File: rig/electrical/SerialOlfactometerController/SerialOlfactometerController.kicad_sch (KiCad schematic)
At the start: 34 parts, among them J1 Screw_Terminal_01x02, J10 Screw_Terminal_01x02, J11 Screw_Terminal_01x02, J12 Screw_Terminal_01x02, J13 Screw_Terminal_01x02, J14 Screw_Terminal_01x02, J15 Screw_Terminal_01x02, J16 Screw_Terminal_01x02, J17 Conn_01x05_Socket, J18 TST-105-01-X-D, J19 TST-105-01-X-D, J2 Screw_Terminal_01x02, J3 Screw_Terminal_01x02, J4 Screw_Terminal_01x02, J5 Screw_Terminal_01x02, J6 Screw_Terminal_01x02, J7 Screw_Terminal_01x02, J8 Screw_Terminal_01x02, J9 Screw_Terminal_01x02, U1 TPIC6595, U2 TPIC6595

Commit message: Serial Olfactometer improved design
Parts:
- added TP1, TP2, TP3, TP4, TP5, TP6: TestPoint, TestPoint:TestPoint_Pad_2.0x2.0mm, symbol Connector:TestPoint
- R3, R4, R5, R6, R7: value R -> 33Ω
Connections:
- net at J19.01, R7.2, U1.13 (SRCK)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: now also TP2.1, TP6.1
- net at J17.5 (Pin_5), U1.12 (RCLK), U2.12 (RCLK): now also TP3.1
- net at U1.18 (SER_OUT), U2.3 (SER_IN): now also TP4.1
- net at J18.03, U1.3 (SER_IN): now also TP1.1
- net at J19.03, U2.18 (SER_OUT): now also TP5.1
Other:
- company: (none) -> Ruta and Kronauer Labs, Rockefeller University
- title: (none) -> MultiBiOS Serial Olfactometer Controller
- moved on the sheet: C1, C2, C3, C4, H1, H2, J1, J10, J11, J12, J13, J14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

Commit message: Update SerialOlfactometerController.kicad_sch
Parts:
- removed H1, H2: MountingHole, MountingHole:MountingHole_3.2mm_M3_DIN965_Pad, symbol Mechanical:MountingHole
- added H3, H4: MountingHole_Pad, symbol Mechanical:MountingHole_Pad
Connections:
- net GND: now also H3.1, H4.1
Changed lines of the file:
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@@
 	)
 	(junction
+		(at 170.18 157.48)
+		(diameter 0)
+		(color 0 0 0 0)
+	)
+	(junction
 		(at 130.81 153.67)
 		(diameter 0)
@@
 	(wire
 		(pts
+			(xy 163.83 157.48) (xy 163.83 158.75)
+		)
+		(stroke
+			(width 0)
+			(type default)
+		)
+	)
+	(wire
+		(pts
 			(xy 114.3 137.16) (xy 114.3 133.35)
 		)
@@
 	(wire
 		(pts
+			(xy 170.18 157.48) (xy 163.83 157.48)
+		)
+		(stroke
+			(width 0)
+			(type default)
+		)
+	)
+	(wire
+		(pts
 			(xy 50.8 158.75) (xy 50.8 165.1)
 		)
@@
 	(wire
 		(pts
+			(xy 173.99 166.37) (xy 170.18 166.37)
+		)
+		(stroke
+			(width 0)
+			(type default)
+		)
+	)
+	(wire
+		(pts
 			(xy 156.21 130.81) (xy 175.26 130.81)
 		)
@@
 	(wire
 		(pts
+			(xy 173.99 157.48) (xy 170.18 157.48)
+		)
+		(stroke
+			(width 0)
+			(type default)
+		)
+	)
+	(wire
+		(pts
 			(xy 91.44 172.72) (xy 91.44 186.69)
 		)
@@
 	(wire
 		(pts
+			(xy 170.18 157.48) (xy 170.18 166.37)
+		)
+		(stroke
+			(width 0)
+			(type default)
+		)
+	)
+	(wire
+		(pts
 			(xy 50.8 165.1) (xy 52.07 165.1)
 		)
@@
 	)
 	(symbol
+		(lib_id "power:GND")
+		(at 163.83 158.75 0)
+		(unit 1)
+		(exclude_from_sim no)
+		(in_bom yes)
+		(on_board yes)
+		(dnp no)
+		(fields_autoplaced yes)
+		(property "Reference" "#PWR035"
+			(at 163.83 165.1 0)
+			(effects
+				(font
+					(size 1.27 1.27)
+				)
+				(hide yes)
+			)
+		)
+		(property "Value" "GND"
+			(at 163.83 163.83 0)
+			(effects
+				(font
+					(size 1.27 1.27)
+				)
+			)
+		)
+		(property "Footprint" ""
+			(at 163.83 158.75 0)
+			(effects
+				(font
+					(size 1.27 1.27)
+				)
+				(hide yes)
+			)
+		)
+		(property "Datasheet" ""
+			(at 163.83 158.75 0)
+			(effects
+				(font
+					(size 1.27 1.27)
+				)
+				(hide yes)
+			)
+		)
+		(property "Description" "Power symbol creates a global label with name \"GND\" , ground"
+			(at 163.83 158.75 0)
+			(effects
+				(font
+					(size 1.27 1.27)
+				)
+				(hide yes)
+			)
+		)
+		(pin "1"
+		)
+		(instances
+			(project "SerialOlfactometerController"
+				(path "/50fb9429-008b-4a20-9c95-cf3891060a53"
+					(reference "#PWR035")
+					(unit 1)
+				)
+			)
+		)
+	)
+	(symbol
 		(lib_id "Connector:Screw_Terminal_01x02")
 		(at 118.11 77.47 90)
@@
 	)
 	(symbol
-		(lib_id "Mechanical:MountingHole")
-		(at 151.13 161.29 0)
-		(unit 1)
-		(exclude_from_sim no)
-		(in_bom no)
-		(on_board yes)
-		(dnp no)
-		(fields_autoplaced yes)
-		(property "Reference" "H2"
-			(at 153.67 160.0199 0)
-			(effects
-				(font
-					(size 1.27 1.27)
-				)
-				(justify left)
-			)
-		)
-		(property "Value" "MountingHole"
-			(at 153.67 162.5599 0)
-			(effects
-				(font
-					(size 1.27 1.27)
-				)
-				(justify left)
-			)
-		)
-		(property "Footprint" "MountingHole:MountingHole_3.2mm_M3_DIN965_Pad"
-			(at 151.13 161.29 0)
-			(effects
-				(font
-					(size 1.27 1.27)
-				)
-				(hide yes)
-			)
-		)
-		(property "Datasheet" "~"
-			(at 151.13 161.29 0)
-			(effects
-				(font
-					(size 1.27 1.27)
-				)
-				(hide yes)
-			)
-		)
-		(property "Description" "Mounting Hole without connection"
-			(at 151.13 161.29 0)
-			(effects
-				(font
-					(size 1.27 1.27)
-				)
-				(hide yes)
-			)
-		)
-		(instances
-			(project ""
-				(path "/50fb9429-008b-4a20-9c95-cf3891060a53"
-					(reference "H2")
-					(unit 1)
-				)
-			)
-		)
-	)
-	(symbol
 		(lib_id "Connector:TestPoint")
 		(at 130.81 153.67 0)
@@
 	)
 	(symbol
-		(lib_id "Mechanical:MountingHole")
-		(at 151.13 153.67 0)
-		(unit 1)
-		(exclude_from_sim no)
-		(in_bom no)
-		(on_board yes)
-		(dnp no)
-		(fields_autoplaced yes)
-		(property "Reference" "H1"
-			(at 153.67 152.3999 0)
-			(effects
-				(font
-					(size 1.27 1.27)
-				)
-				(justify left)
-			)
-		)
-		(property "Value" "MountingHole"
-			(at 153.67 154.9399 0)
-			(effects
-				(font
-					(size 1.27 1.27)
-				)
-				(justify left)
-			)
-		)
-		(property "Footprint" "MountingHole:MountingHole_3.2mm_M3_DIN965_Pad"
-			(at 151.13 153.67 0)
-			(effects
-				(font
-					(size 1.27 1.27)
-				)
-				(hide yes)
-			)
-		)
-		(property "Datasheet" "~"
-			(at 151.13 153.67 0)
-			(effects
-				(font
-					(size 1.27 1.27)
-				)
-				(hide yes)
-			)
-		)
-		(property "Description" "Mounting Hole without connection"
-			(at 151.13 153.67 0)
-			(effects
-				(font
-					(size 1.27 1.27)
-				)
-				(hide yes)
-			)
-		)
-		(instances
-			(project ""
-				(path "/50fb9429-008b-4a20-9c95-cf3891060a53"
-					(reference "H1")
-					(unit 1)
-				)
-			)
-		)
-	)
-	(symbol
 		(lib_id "Connector:Screw_Terminal_01x02")
 		(at 124.46 80.01 90)
@@
 	)
 	(symbol
+		(lib_id "Mechanical:MountingHole_Pad")
+		(at 173.99 154.94 0)
+		(unit 1)
+		(exclude_from_sim no)
+		(in_bom no)
+		(on_board yes)
+		(dnp no)
+		(fields_autoplaced yes)
+		(property "Reference" "H3"
+			(at 176.53 152.3999 0)
+			(effects
+				(font
+					(size 1.27 1.27)
+				)
+				(justify left)
+			)
+		)
+		(property "Value" "MountingHole_Pad"
+			(at 176.53 154.9399 0)
+			(effects
+				(font
+					(size 1.27 1.27)
+				)
+				(justify left)
+			)
+		)
+		(property "Footprint" ""
+			(at 173.99 154.94 0)
+			(effects
+				(font
+					(size 1.27 1.27)
+				)
+				(hide yes)
+			)
+		)
+		(property "Datasheet" "~"
+			(at 173.99 154.94 0)
+			(effects
+				(font
+					(size 1.27 1.27)
+				)
+				(hide yes)
+			)
+		)
+		(property "Description" "Mounting Hole with connection"
+			(at 173.99 154.94 0)
+			(effects
+				(font
+					(size 1.27 1.27)
+				)
+				(hide yes)
+			)
+		)
+		(pin "1"
+		)
+		(instances
+			(project ""
+				(path "/50fb9429-008b-4a20-9c95-cf3891060a53"
+					(reference "H3")
+					(unit 1)
+				)
+			)
+		)
+	)
+	(symbol
 		(lib_id "Connector:Screw_Terminal_01x02")
 		(at 111.76 85.09 90)
@@
 					(unit 1)
 				)
+			)
+		)
+	)
+	(symbol
+		(lib_id "Mechanical:MountingHole_Pad")
+		(at 173.99 163.83 0)
+		(unit 1)
+		(exclude_from_sim no)
+		(in_bom no)
+		(on_board yes)
+		(dnp no)
+		(fields_autoplaced yes)
+		(property "Reference" "H4"
+			(at 176.53 161.2899 0)
+			(effects
+				(font
+					(size 1.27 1.27)
+				)
+				(justify left)
+			)
+		)
+		(property "Value" "MountingHole_Pad"
+			(at 176.53 163.8299 0)
+			(effects
+				(font
+					(size 1.27 1.27)
+				)
+				(justify left)
+			)
+		)
+		(property "Footprint" ""
+			(at 173.99 163.83 0)
+			(effects
+				(font
+					(size 1.27 1.27)
+				)
+				(hide yes)
+			)
+		)
+		(property "Datasheet" "~"
+			(at 173.99 163.83 0)
+			(effects
+				(font
+					(size 1.27 1.27)
+				)
+				(hide yes)
+			)
+		)
+		(property "Description" "Mounting Hole with connection"
+			(at 173.99 163.83 0)
+			(effects
+				(font
+					(size 1.27 1.27)
+				)
+				(hide yes)
+			)
+		)
+		(pin "1"
+		)
+		(instances
+			(project ""
+				(path "/50fb9429-008b-4a20-9c95-cf3891060a53"
+					(reference "H4")
+					(unit 1)
+				)

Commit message: Tweaking of v1 boards
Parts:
- H3, H4: footprint (none) -> MountingHole:MountingHole_3.2mm_M3_Pad
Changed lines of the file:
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@@
 			)
 		)
-		(property "Footprint" ""
+		(property "Footprint" "MountingHole:MountingHole_3.2mm_M3_Pad"
 			(at 173.99 154.94 0)
 			(effects
@@
 			)
 		)
-		(property "Footprint" ""
+		(property "Footprint" "MountingHole:MountingHole_3.2mm_M3_Pad"
 			(at 173.99 163.83 0)
 			(effects

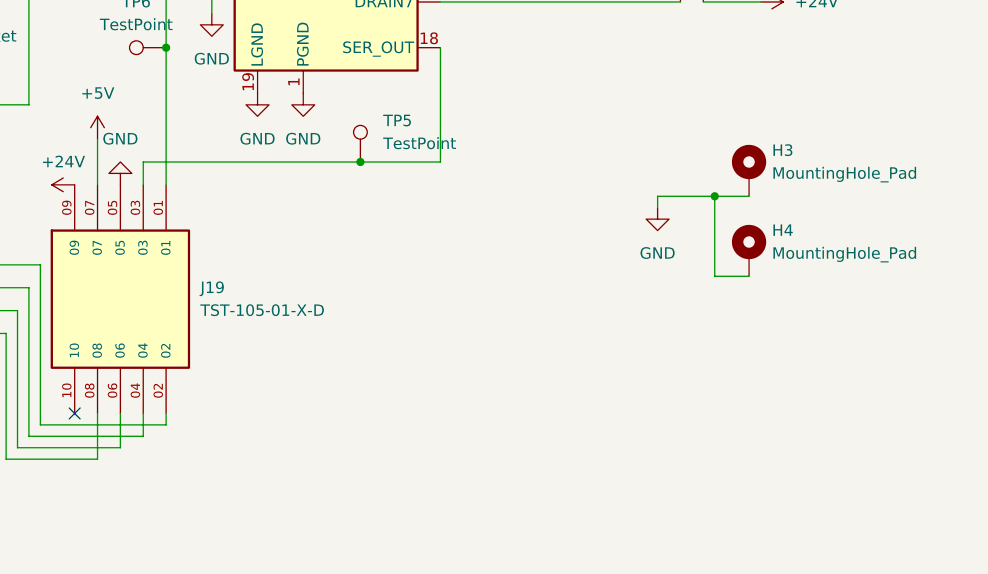
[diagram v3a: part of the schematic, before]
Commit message: Termination Resistors/GND Vias
Added termination resistors to avoid reflections on signal lines. Added vias to GND plane stubs to avoid antennae effects.
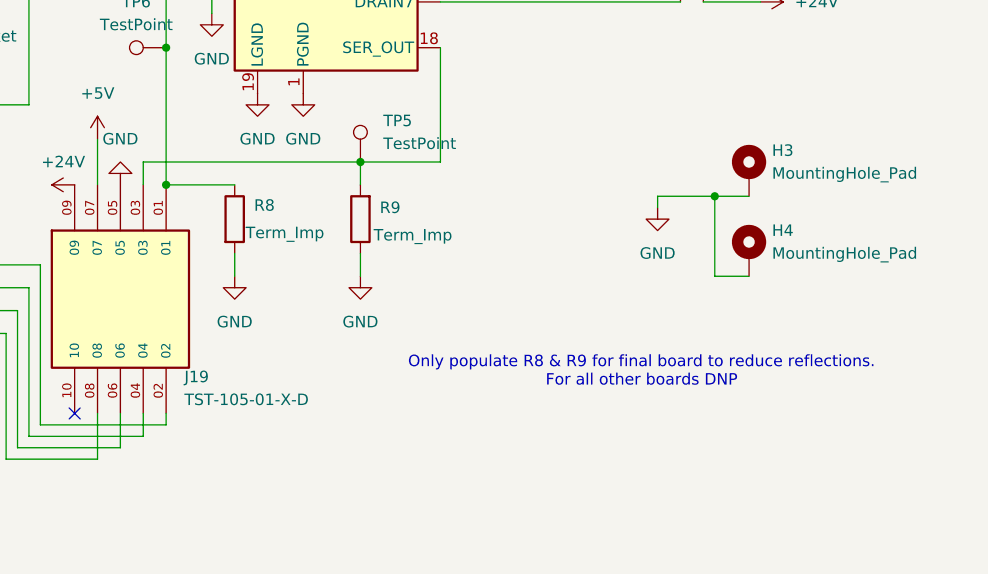
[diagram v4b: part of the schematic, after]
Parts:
- added R8, R9: Term_Imp, Resistor_SMD:R_0603_1608Metric, symbol Device:R
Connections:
- net GND: now also R8.2, R9.1
- net at J19.01, R7.2, TP2.1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: now also R8.1
- net at J19.03, TP5.1, U2.18 (SER_OUT): now also R9.2
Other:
- note added: "Only populate R8 & R9 for final board to reduce reflections. For all other boards DNP"
